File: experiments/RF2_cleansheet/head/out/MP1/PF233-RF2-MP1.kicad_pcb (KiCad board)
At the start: 2 copper layers, 26 x 36 mm, 24 parts, among them J1 COIL_A, J2 COIL_B, J3 MONO_OUT, J4 +5VA, J5 AGND, U1 OPA2211AIDR

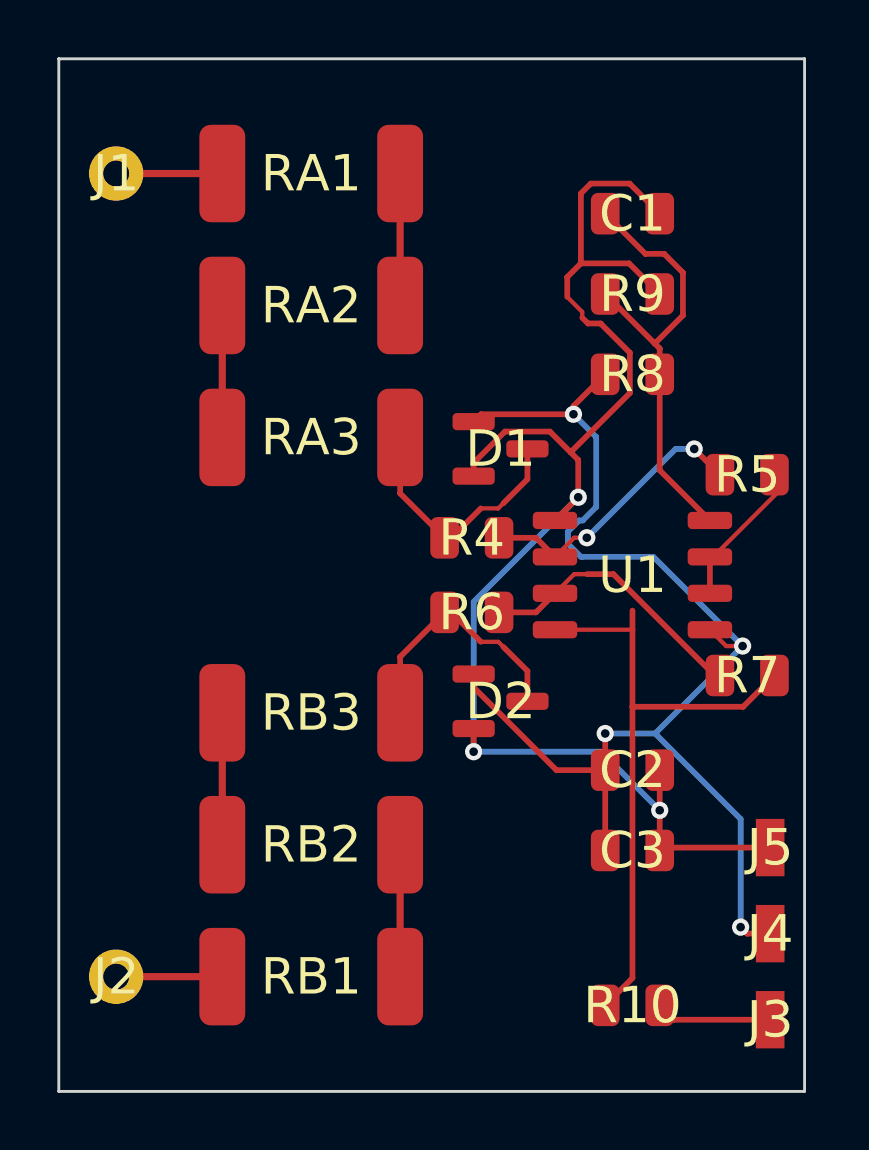
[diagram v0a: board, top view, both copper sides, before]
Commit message: RF2: LED ring LR1 routed by a deterministic template (no autorouter), sign-off PASS
- rf2_ring_template.py: one cell per LED (data outer lane, clock inner lane, never crossing on a layer), chain links, power stubs to the open B.Cu buses, B.Cu crossings under the radial hinge feeds, and the 4 irregular links (hinge feeds, outer-to-inner jump). LR1: KiCad DRC 0, 0 unconnected, min clearance 0.19 mm (rule 0.10), no loop around the axis, parity, Gerbers; builds in 14 s. Freerouting had stalled (no pass in 5 min for 4 connections)
- netlist: LR1 capacitors rotated (+5V pin on the VDD side), hinge lands JH3 = clock / JH4 = data (harness C10c/C10d follow)
- rf2_boards: no autorouter run when nothing is open (template, pre-routes or resumed copper); board-setup via minima and a .kicad_dru written beside each board; freeroute --no-fanout for resumes
- rf2_head: LED envelope no longer empty (zero-height solid), capacitor sites added
- sign-off order: ledger before the housing checks. Head mass corrected 702 -> 745 g (docs/CORRECTIONS.md)
- Freerouting scratch folders untracked

Co-Authored-By: Claude Opus 5.5 <noreply@anthropic.com>
Claude-Session: https://claude.ai/code/session_01FX4DWSYYjMCFGGA6gmha65
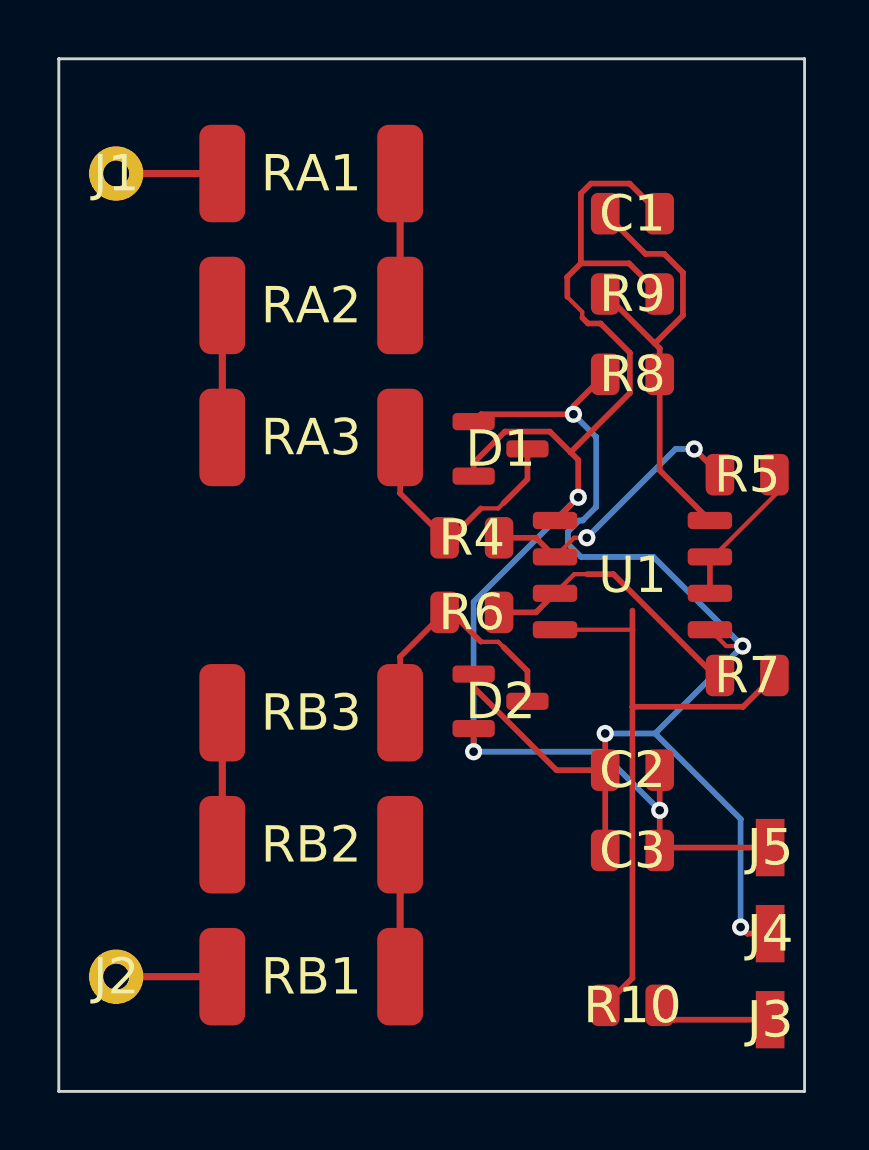
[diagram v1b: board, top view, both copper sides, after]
